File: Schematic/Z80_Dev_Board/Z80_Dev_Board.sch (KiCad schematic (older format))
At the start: 8 parts

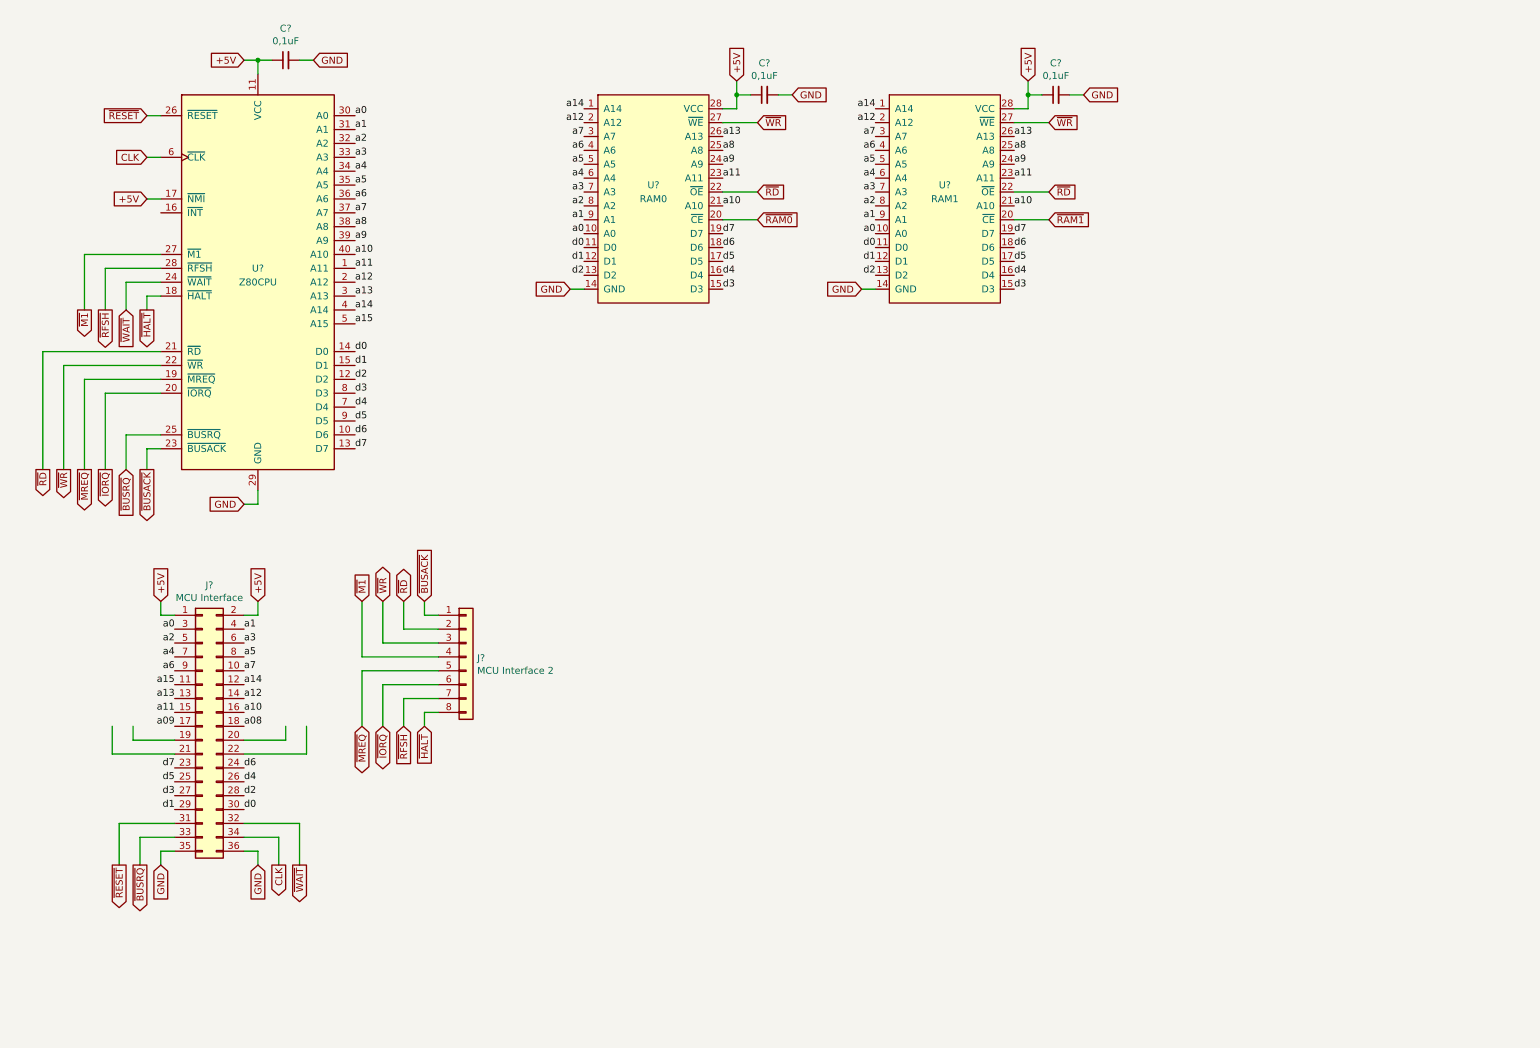
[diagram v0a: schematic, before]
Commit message: Added basic glue logic and clock toggle circuit
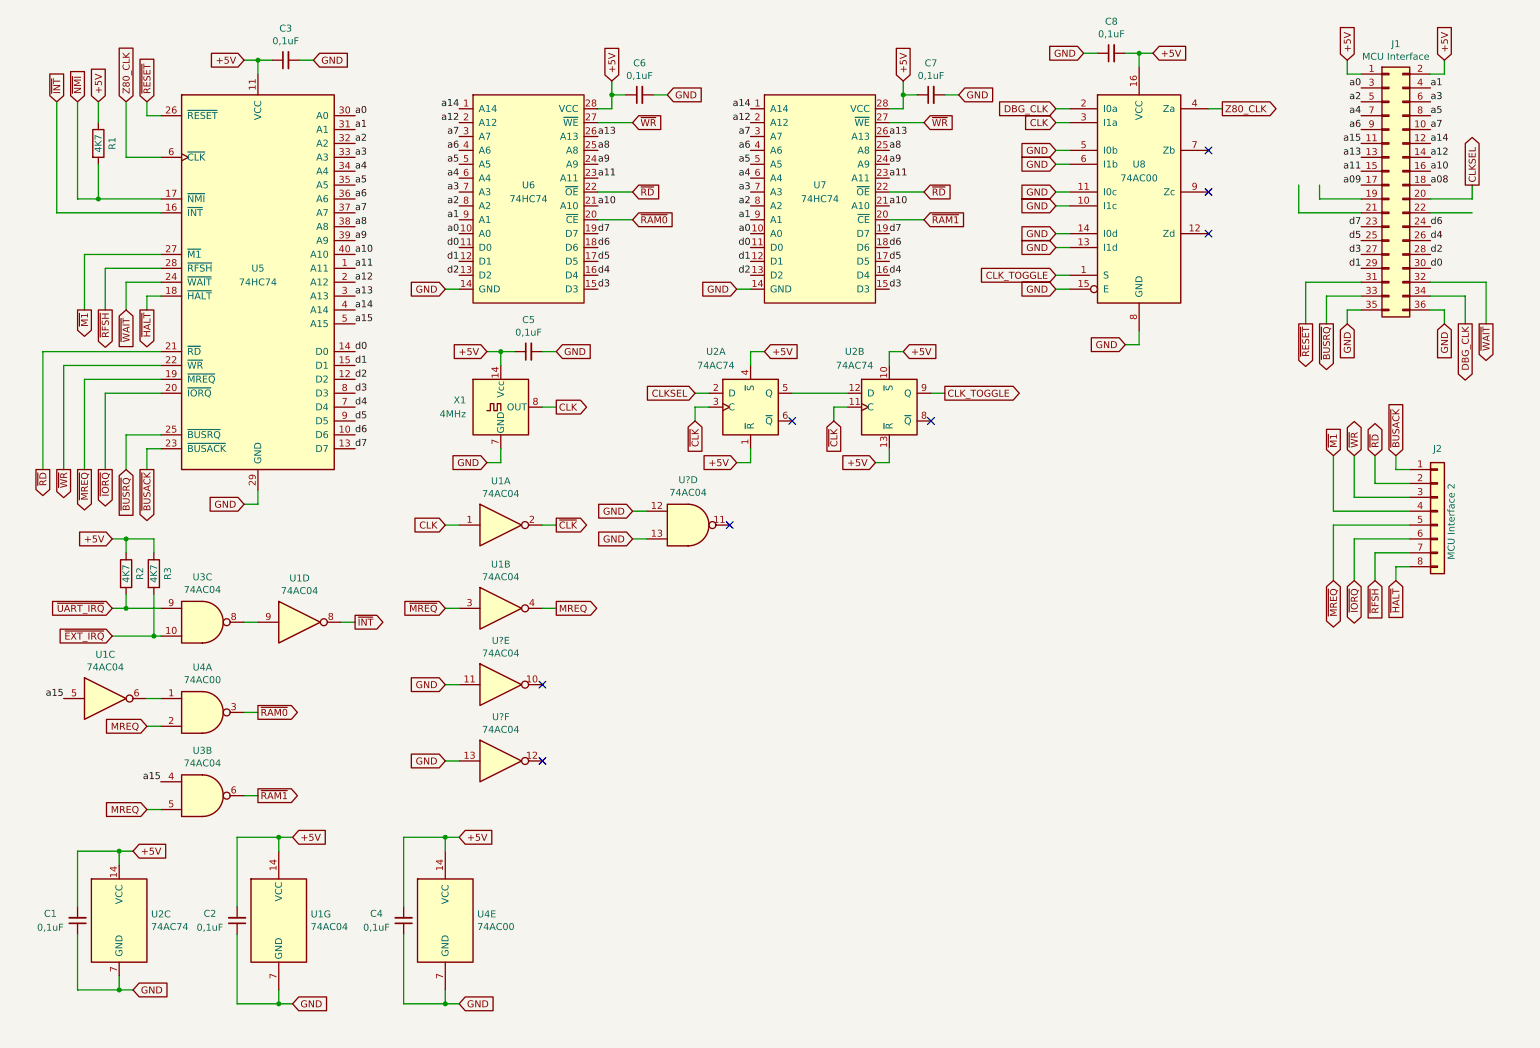
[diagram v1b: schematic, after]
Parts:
- added C1, C2, C4, C5, C8: 0,1uF, symbol Device:C_Small
- added R1, R2, R3: 4K7, symbol Device:R
- added U1, U? (x2): 74AC04, symbol 74xx:74HC04
- added U2: 74AC74, symbol 74xx:74HC74
- added U3, U?: 74AC04, symbol 74xx:74HC00
- added U4: 74AC00, symbol 74xx:74HC00
- added U8: 74AC00, symbol 74xx:74LS157
- added X1: 4MHz, Oscillator:Oscillator_DIP-14, symbol Oscillator:DGOF5S3
- U5: renamed from U?; value Z80CPU -> 74HC74
- U6: renamed from U?; value RAM0 -> 74HC74; footprint Package_DIP:DIP-28_W15.24mm_Socket -> (none)
- U7: renamed from U?; value RAM1 -> 74HC74; footprint Package_DIP:DIP-28_W15.24mm_Socket -> (none)
- gave numbers to parts that had none: 5
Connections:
- net labels added: CLKSEL, CLK_TOGGLE, DBG_CLK, MREQ, Z80_CLK, ~CLK, ~EXT_IRQ, ~INT, ~NMI, ~UART_IRQ
- wire segments 87 -> 182
- no-connect marks 0 -> 8
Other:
- moved on the sheet: C6, C7, J1, J2, U6, U7

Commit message: Completed basic schematic
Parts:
- added C10, C5: 0,1uF, Capacitor_THT:C_Disc_D5.0mm_W2.5mm_P2.50mm, symbol Device:C_Small
- added C11, C12: 22pF, Capacitor_THT:C_Disc_D5.0mm_W2.5mm_P2.50mm, symbol Device:C_Small
- added J1: Conn_02x18_Odd_Even, Connector_PinHeader_2.54mm:PinHeader_2x18_P2.54mm_Vertical, symbol Connector_Generic:Conn_02x18_Odd_Even
- added J3: UART B, Connector_PinHeader_2.54mm:PinHeader_1x06_P2.54mm_Horizontal, symbol Connector_Generic:Conn_01x06
- added J5: UART A, Connector_PinHeader_2.54mm:PinHeader_1x06_P2.54mm_Horizontal, symbol Connector_Generic:Conn_01x06
- added U3: 74AC08, Package_DIP:DIP-14_W7.62mm_Socket, symbol 74xx:74LS08
- added U9: SC26C92, Package_LCC:PLCC-44_THT-Socket, symbol 6502:SC26C92
- added Y1: 3,6864 MHz, Crystal:Crystal_HC49-U_Vertical, symbol Device:Crystal_Small
- C1, C2, C3, C4: footprint (none) -> Capacitor_THT:C_Disc_D5.0mm_W2.5mm_P2.50mm
- C6: renamed from C5; footprint (none) -> Capacitor_THT:C_Disc_D5.0mm_W2.5mm_P2.50mm
- C7: renamed from C6; footprint (none) -> Capacitor_THT:C_Disc_D5.0mm_W2.5mm_P2.50mm
- C8: renamed from C7; footprint (none) -> Capacitor_THT:C_Disc_D5.0mm_W2.5mm_P2.50mm
- C9: renamed from C8; footprint (none) -> Capacitor_THT:C_Disc_D5.0mm_W2.5mm_P2.50mm
- J2: footprint (none) -> Connector_PinHeader_2.54mm:PinHeader_1x08_P2.54mm_Vertical
- R1, R2, R3: footprint (none) -> Resistor_THT:R_Axial_DIN0207_L6.3mm_D2.5mm_P10.16mm_Horizontal
- U1, U2, U4: footprint (none) -> Package_DIP:DIP-14_W7.62mm_Socket
- U1: renamed from U?; footprint (none) -> Package_DIP:DIP-14_W7.62mm_Socket
- U4: renamed from U3; value 74AC04 -> 74AC00; footprint (none) -> Package_DIP:DIP-14_W7.62mm_Socket
- U4: renamed from U?; value 74AC04 -> 74AC00; footprint (none) -> Package_DIP:DIP-14_W7.62mm_Socket
- U5: value 74HC74 -> Z80 CPU; footprint (none) -> Package_DIP:DIP-40_W15.24mm_Socket
- U6, U7: value 74HC74 -> 62256; footprint (none) -> Package_DIP:DIP-28_W7.62mm_Socket
- U8: value 74AC00 -> 74HC157; footprint (none) -> Package_DIP:DIP-16_W7.62mm_Socket
- renumbered J1 to J4
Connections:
- net a08 is gone; now on net a8: J4.18 (Pin_18)
- net a09 is gone; now on net a9: J4.17 (Pin_17)
- net +5V: now also C10.1, C5.2, J1.34 (Pin_34), U3.14 (VCC), U9.44 (VCC)
- net CLKSEL: now also J4.19 (Pin_19); no longer J4.20 (Pin_20)
- net GND: now also U1.13, U4.12, U4.13, C10.2, C11.1, C12.2, C5.1, J1.36 (Pin_36), J3.1 (Pin_1), J5.1 (Pin_1), U3.10, U3.12, U3.13, U3.7 (GND), U3.9, U9.22 (VSS); no longer U1.11, U1.13, U4.12, U4.13
- net Z80_CLK: now also J1.17 (Pin_17)
- net a0: now also J1.2 (Pin_2), U9.2 (A0)
- net a1: now also J1.4 (Pin_4), U9.4 (A1)
- net a10: now also J1.22 (Pin_22)
- net a11: now also J1.24 (Pin_24)
- net a12: now also J1.26 (Pin_26)
- net a13: now also J1.28 (Pin_28)
- net a14: now also J1.30 (Pin_30)
- net a15: now also U4.10, J1.32 (Pin_32)
- net a2: now also J1.6 (Pin_6), U9.6 (A2)
- net a3: now also J1.8 (Pin_8), U9.7 (A3)
- net a4: now also J1.10 (Pin_10)
- net a5: now also J1.12 (Pin_12)
- net a6: now also J1.14 (Pin_14)
- net a7: now also J1.16 (Pin_16)
- net a8: now also J1.18 (Pin_18)
- net a9: now also J1.20 (Pin_20)
- net d0: now also J1.1 (Pin_1), U9.28 (D0)
- net d1: now also J1.3 (Pin_3), U9.18 (D1)
- net d2: now also J1.5 (Pin_5), U9.27 (D2)
- net d3: now also J1.7 (Pin_7), U9.19 (D3)
- net d4: now also J1.9 (Pin_9), U9.26 (D4)
- net d5: now also J1.11 (Pin_11), U9.20 (D5)
- net d6: now also J1.13 (Pin_13), U9.25 (D6)
- net d7: now also J1.15 (Pin_15), U9.21 (D7)
- net ~BUSACK: now also J1.31 (Pin_31)
- net ~BUSRQ: now also U3.6; no longer J4.33 (Pin_33)
- net ~EXT_IRQ: now also J1.33 (Pin_33), U3.2; no longer U4.10
- net ~INT: now also U3.3; no longer U1.8
- net ~IORQ: now also U1.11, J1.27 (Pin_27)
- net ~MREQ: now also J1.25 (Pin_25)
- net ~NMI: now also J1.35 (Pin_35)
- net ~RD: now also J1.21 (Pin_21), U9.10 (RDN)
- net ~RESET: now also U1.9, J1.19 (Pin_19)
- net ~UART_IRQ: now also U3.1, U9.24 (INTRN); no longer U4.9
- net ~WR: now also J1.23 (Pin_23), U9.9 (WRN)
- new net: C12.1, U9.36 (X1/CLK), Y1.2
- new net: C11.2, U9.37 (X2), Y1.1
- new net IORQ: U1.10, U4.9
- new net RESET: U1.8, U9.38 (RESET)
- new net UARTA_RxD: J5.4 (Pin_4), U9.35 (RxDA)
- new net UARTA_TxD: J5.5 (Pin_5), U9.33 (TxDA)
- new net UARTA_~CTS: J5.6 (Pin_6), U9.8 (IP0)
- new net UARTA_~RTS: J5.2 (Pin_2), U9.32 (OP0)
- new net UARTB_RxD: J3.4 (Pin_4), U9.11 (RxDB)
- new net UARTB_TxD: J3.5 (Pin_5), U9.13 (TxDB)
- new net UARTB_~CTS: J3.6 (Pin_6), U9.5 (IP1)
- new net UARTB_~RTS: J3.2 (Pin_2), U9.14 (OP1)
- new net ~DBG_BUSRQ: J4.33 (Pin_33), U3.4
- new net ~EXT_BUSRQ: J1.29 (Pin_29), U3.5
- new net ~UART: U4.8, U9.39 (CEN)
- no-connect marks 8 -> 25
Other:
- moved on the sheet: C1, C2, C4, C6, C7, C8, J2, R2, R3, U1A, U1B, U1C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

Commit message: Updated schematic
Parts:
- added C9: 10uF, Capacitor_THT:CP_Radial_D5.0mm_P2.50mm, symbol Device:CP_Small
- added J2: GPIO, Connector_PinSocket_2.54mm:PinSocket_1x11_P2.54mm_Vertical, symbol Connector_Generic:Conn_01x11
- added R4, R5, R6, R7, R8, R9: 4K7, Resistor_THT:R_Axial_DIN0207_L6.3mm_D2.5mm_P10.16mm_Horizontal, symbol Device:R
- J1: value Conn_02x18_Odd_Even -> Expansion port
- U6, U7: footprint Package_DIP:DIP-28_W7.62mm_Socket -> Package_DIP:DIP-28_W15.24mm_Socket
- renumbered C9 to C10, C10 to C11, C11 to C12, C12 to C13, J2 to J3, J3 to J4, J4 to J5, J5 to J6
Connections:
- net +5V: now also C9.1, R4.1, R5.1, R9.2; no longer U2.1 (~R), U2.13 (~R)
- net CLKSEL: now also R7.1
- net DBG_CLK: now also R8.1
- net GND: now also C9.2, R6.2, R7.2, R8.2
- net ~DBG_BUSRQ: now also R4.2
- net ~EXT_BUSRQ: now also R5.2
- net ~RESET: now also U2.1 (~R), U2.13 (~R), R6.1
- net ~WAIT: now also R9.1
- net op3: now reaches U9.15 (OP3)
- net op3: now also J2.7 (Pin_7)
- net op5: now reaches U9.16 (OP5)
- net op5: now also J2.9 (Pin_9)
- net op7: now reaches U9.17 (OP7)
- net op7: now also J2.11 (Pin_11)
- net op6: now reaches U9.29 (OP6)
- net op6: now also J2.10 (Pin_10)
- net ip3: now reaches U9.3 (IP3)
- net ip3: now also J2.2 (Pin_2)
- net op4: now reaches U9.30 (OP4)
- net op4: now also J2.8 (Pin_8)
- net op2: now reaches U9.31 (OP2)
- net op2: now also J2.6 (Pin_6)
- net ip2: now reaches U9.40 (IP2)
- net ip2: now also J2.1 (Pin_1)
- net ip6: now reaches U9.41 (IP6)
- net ip6: now also J2.5 (Pin_5)
- net ip5: now reaches U9.42 (IP5)
- net ip5: now also J2.4 (Pin_4)
- net ip4: now reaches U9.43 (IP4)
- net ip4: now also J2.3 (Pin_3)
- no-connect marks 25 -> 14
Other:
- moved on the sheet: J3, U3B, U4C

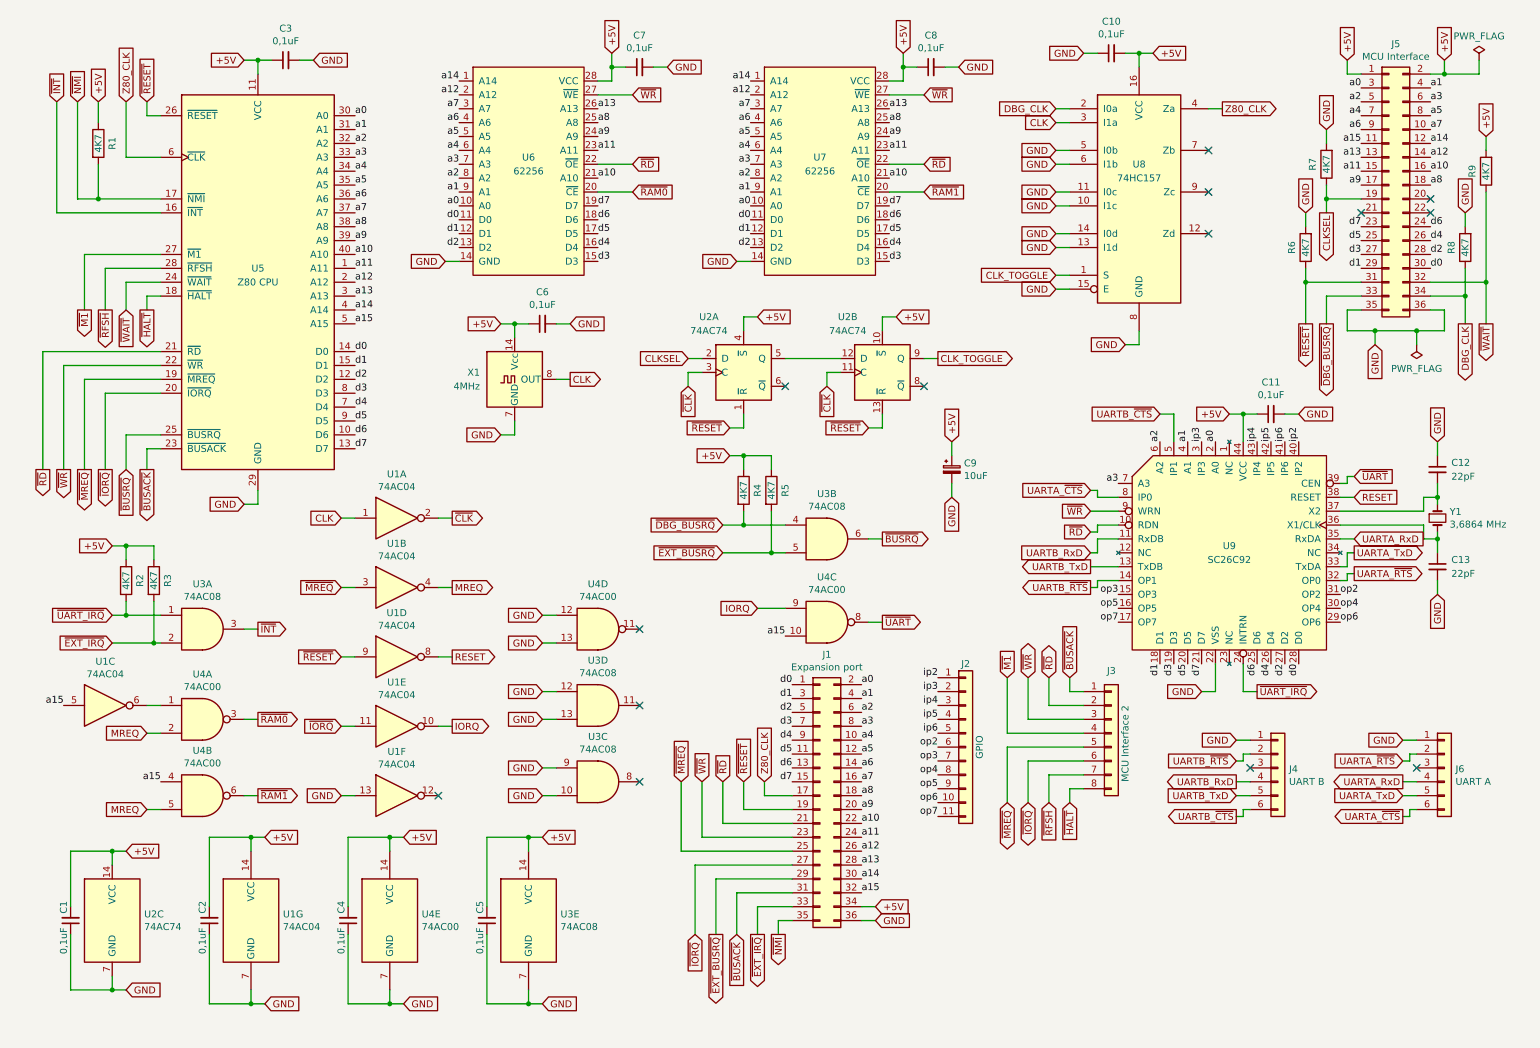
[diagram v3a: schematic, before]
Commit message: Added HALT LED, moved things around
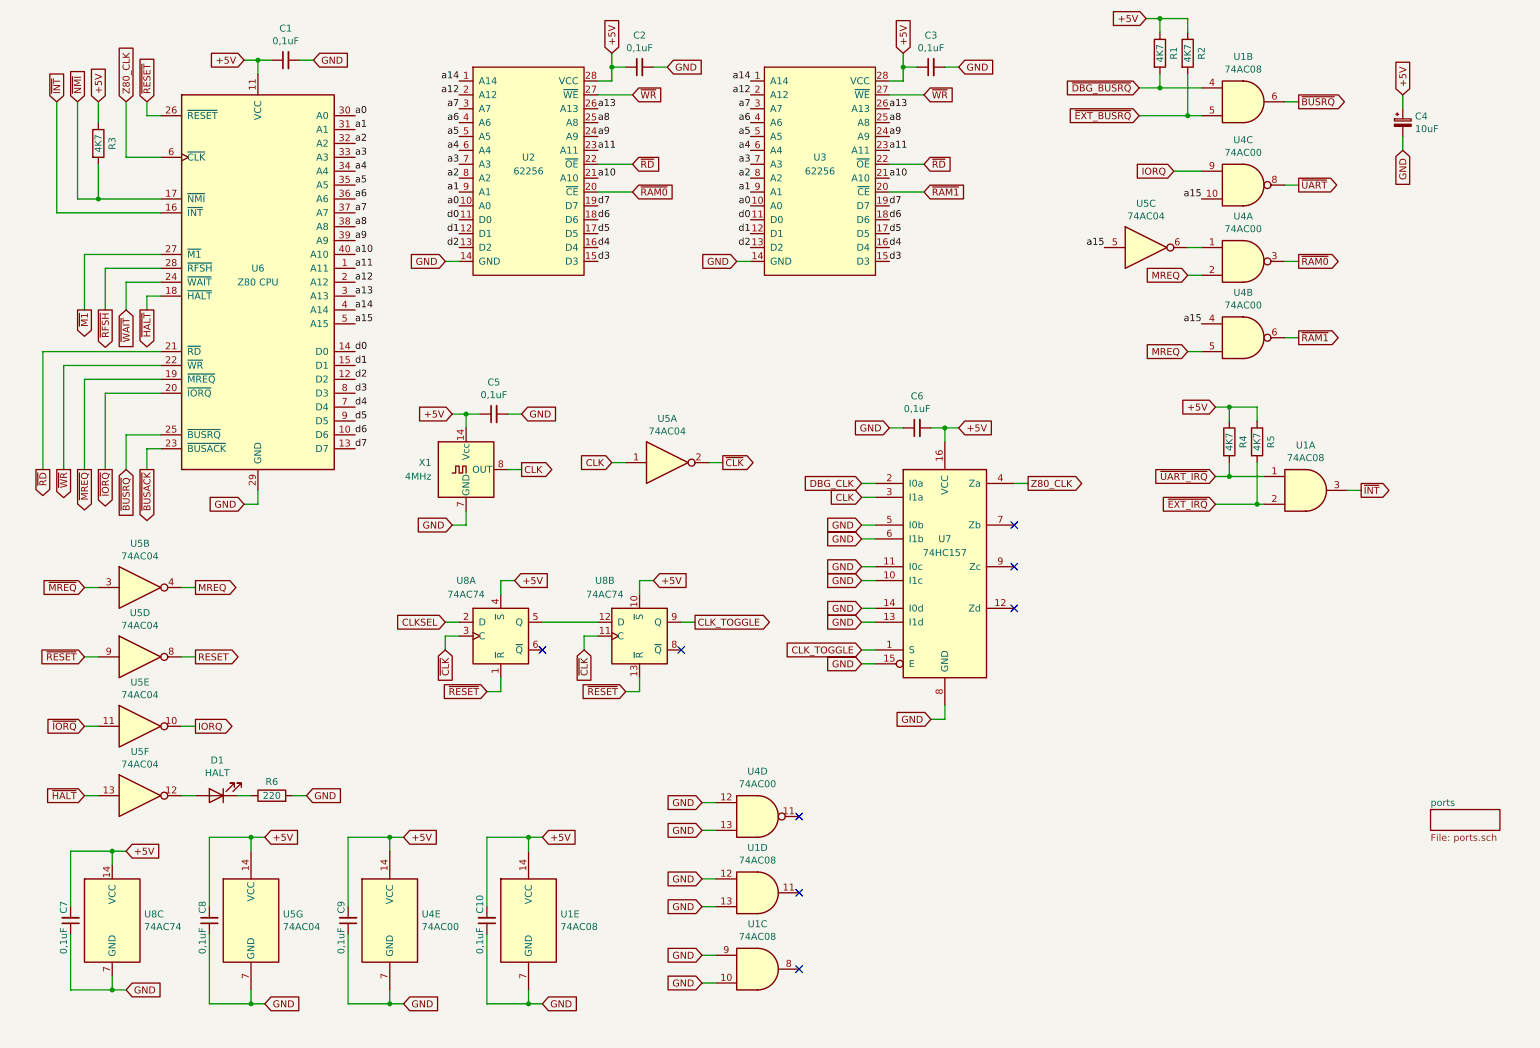
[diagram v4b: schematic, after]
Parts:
- removed C11: 0,1uF, Capacitor_THT:C_Disc_D5.0mm_W2.5mm_P2.50mm, symbol Device:C_Small
- removed C12, C13: 22pF, Capacitor_THT:C_Disc_D5.0mm_W2.5mm_P2.50mm, symbol Device:C_Small
- removed J1: Expansion port, Connector_PinHeader_2.54mm:PinHeader_2x18_P2.54mm_Vertical, symbol Connector_Generic:Conn_02x18_Odd_Even
- removed J2: GPIO, Connector_PinSocket_2.54mm:PinSocket_1x11_P2.54mm_Vertical, symbol Connector_Generic:Conn_01x11
- removed J3: MCU Interface 2, Connector_PinHeader_2.54mm:PinHeader_1x08_P2.54mm_Vertical, symbol Connector_Generic:Conn_01x08
- removed J4: UART B, Connector_PinHeader_2.54mm:PinHeader_1x06_P2.54mm_Horizontal, symbol Connector_Generic:Conn_01x06
- removed J5: MCU Interface, Connector_PinHeader_2.54mm:PinHeader_2x18_P2.54mm_Vertical, symbol Connector_Generic:Conn_02x18_Odd_Even
- removed J6: UART A, Connector_PinHeader_2.54mm:PinHeader_1x06_P2.54mm_Horizontal, symbol Connector_Generic:Conn_01x06
- removed R7, R8, R9: 4K7, Resistor_THT:R_Axial_DIN0207_L6.3mm_D2.5mm_P10.16mm_Horizontal, symbol Device:R
- removed U9: SC26C92, Package_LCC:PLCC-44_THT-Socket, symbol 6502:SC26C92
- removed Y1: 3,6864 MHz, Crystal:Crystal_HC49-U_Vertical, symbol Device:Crystal_Small
- added D1: HALT, LED_THT:LED_D3.0mm_Clear, symbol Device:LED
- R6: value 4K7 -> 220
- renumbered C3 to C1, C5 to C10, C7 to C2, C8 to C3, C9 to C4, C6 to C5, C10 to C6, C1 to C7, C2 to C8, C4 to C9, R4 to R1, R5 to R2, R1 to R3, R2 to R4, R3 to R5, U3 to U1, U6 to U2, U7 to U3, U1 to U5, U5 to U6, U8 to U7, U2 to U8
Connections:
- net GND: no longer U5.13
- net ~HALT: now also U5.13
- net ~RESET: no longer R6.1
- net at U5.12: now also D1.2 (A)
- new net: D1.1 (K), R6.1
- no-connect marks 14 -> 8
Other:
- moved on the sheet: C4, C5, C6, R1, R2, R4, R5, U1A, U1B, U1C, U1D, U4A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
